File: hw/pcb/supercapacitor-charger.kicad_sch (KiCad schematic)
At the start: 11 parts, among them U2 TPS61094

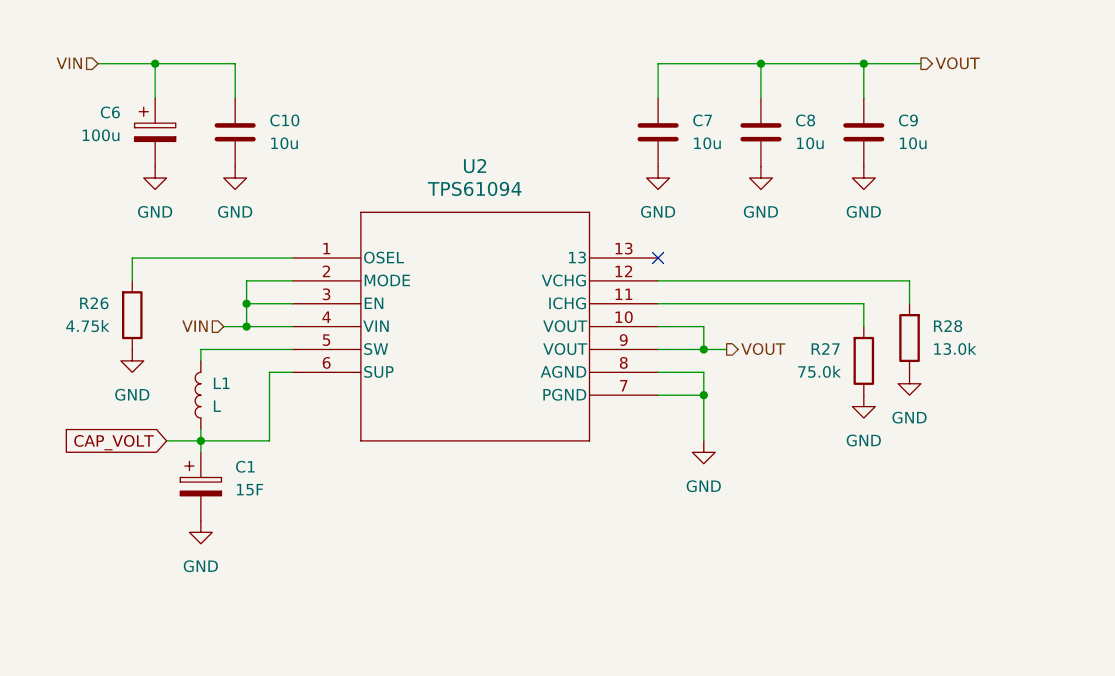
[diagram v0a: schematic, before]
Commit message: chore: updated schematics to show true part numbers
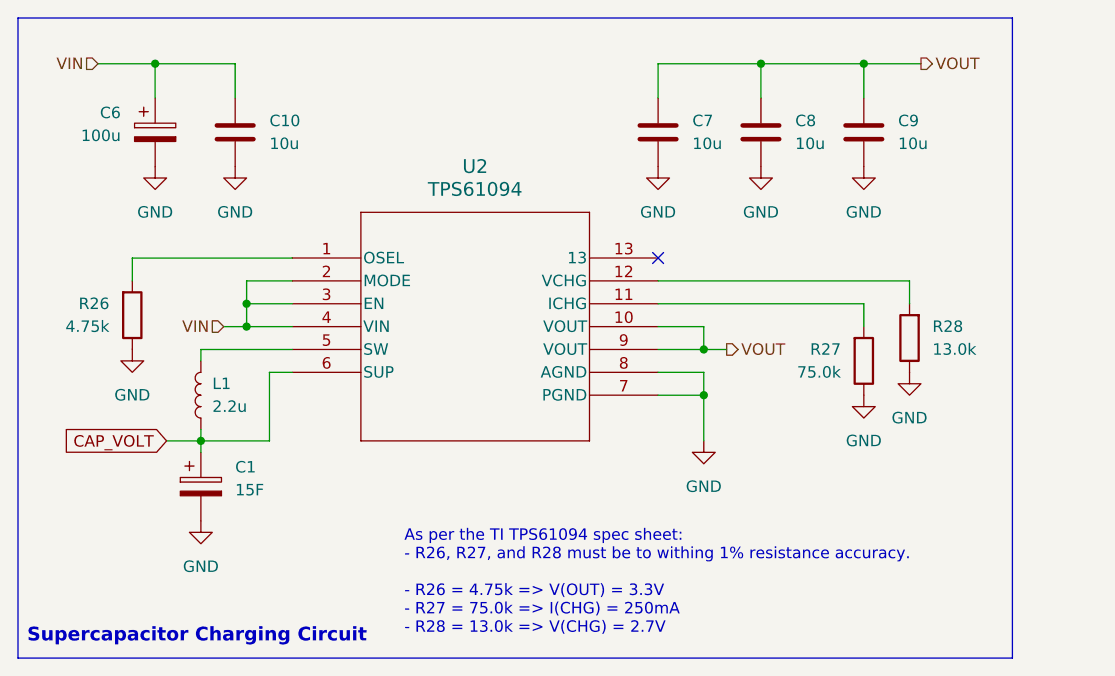
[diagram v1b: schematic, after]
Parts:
- C1: PN (none) -> MAL223051016E3
- C10, C7, C8, C9: PN (none) -> C0805C106K8PACTU
- C6: PN (none) -> UWT1A101MCL1GB
- L1: value L -> 2.2u; PN (none) -> 74438356022
- R26: PN (none) -> CPF0603F4K75C1
- R27: PN (none) -> CPF0603F75KC1
- R28: PN (none) -> CPF0603F13KC1
- U2: PN (none) -> TPS61094DSSR
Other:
- note added: "As per the TI TPS61094 spec sheet: - R26, R27, and R28 must be to withing 1% resistance accuracy. - R26 = 4.75k => V(OUT) = 3.3V - R27 = 75.0k => I(CHG) = 250mA - R28 = 13.0k => V(CHG) = 2.7V"
- note added: "Supercapacitor Charging Circuit"
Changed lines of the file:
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@@
 		(rev "RevA")
+	)
+	(rectangle
+		(start 95.25 71.12)
+		(end 205.74 142.24)
+		(stroke
+			(width 0)
+			(type default)
+		)
+		(fill
+			(type none)
+		)
+	)
+	(text "As per the TI TPS61094 spec sheet:\n- R26, R27, and R28 must be to withing 1% resistance accuracy.\n\n- R26 = 4.75k => V(OUT) = 3.3V\n- R27 = 75.0k => I(CHG) = 250mA\n- R28 = 13.0k => V(CHG) = 2.7V"
+		(exclude_from_sim no)
+		(at 138.176 128.016 0)
+		(effects
+			(font
+				(size 1.27 1.27)
+			)
+			(justify left top)
+		)
+	)
+	(text "Supercapacitor Charging Circuit"
+		(exclude_from_sim no)
+		(at 96.266 140.716 0)
+		(effects
+			(font
+				(size 1.524 1.524)
+				(thickness 0.3048)
+				(bold yes)
+			)
+			(justify left bottom)
+		)
 	)
 	(junction
@@
 			)
 		)
+		(property "PN" "C0805C106K8PACTU"
+			(at 119.38 83.82 0)
+			(hide yes)
+			(show_name no)
+			(do_not_autoplace no)
+			(effects
+				(font
+					(size 1.27 1.27)
+				)
+			)
+		)
 		(pin "1"
 		)
@@
 			)
 		)
+		(property "PN" "CPF0603F75KC1"
+			(at 189.23 109.22 0)
+			(hide yes)
+			(show_name no)
+			(do_not_autoplace no)
+			(effects
+				(font
+					(size 1.27 1.27)
+				)
+			)
+		)
 		(pin "2"
 		)
@@
 			)
 		)
+		(property "PN" "CPF0603F13KC1"
+			(at 194.31 106.68 0)
+			(hide yes)
+			(show_name no)
+			(do_not_autoplace no)
+			(effects
+				(font
+					(size 1.27 1.27)
+				)
+			)
+		)
 		(pin "2"
 		)
@@
 			)
 		)
+		(property "PN" "C0805C106K8PACTU"
+			(at 177.8 83.82 0)
+			(hide yes)
+			(show_name no)
+			(do_not_autoplace no)
+			(effects
+				(font
+					(size 1.27 1.27)
+				)
+			)
+		)
 		(pin "1"
 		)
@@
 		)
 		(property "Description" "Unpolarized capacitor"
+			(at 166.37 83.82 0)
+			(hide yes)
+			(show_name no)
+			(do_not_autoplace no)
+			(effects
+				(font
+					(size 1.27 1.27)
+				)
+			)
+		)
+		(property "PN" "C0805C106K8PACTU"
 			(at 166.37 83.82 0)
 			(hide yes)
@@
 			)
 		)
+		(property "PN" "CPF0603F4K75C1"
+			(at 107.95 104.14 0)
+			(hide yes)
+			(show_name no)
+			(do_not_autoplace no)
+			(effects
+				(font
+					(size 1.27 1.27)
+				)
+			)
+		)
 		(pin "2"
 		)
@@
 			)
 		)
+		(property "PN" "MAL223051016E3"
+			(at 115.57 123.19 0)
+			(hide yes)
+			(show_name no)
+			(do_not_autoplace no)
+			(effects
+				(font
+					(size 1.27 1.27)
+				)
+			)
+		)
 		(pin "2"
 		)
@@
 		)
 		(property "Description" ""
+			(at 146.05 105.41 0)
+			(hide yes)
+			(show_name no)
+			(do_not_autoplace no)
+			(effects
+				(font
+					(size 1.27 1.27)
+				)
+			)
+		)
+		(property "PN" "TPS61094DSSR"
 			(at 146.05 105.41 0)
 			(hide yes)
@@
 			)
 		)
-		(property "Value" "L"
+		(property "Value" "2.2u"
 			(at 116.84 114.2999 0)
 			(show_name no)
@@
 		)
 		(property "Description" "Inductor"
+			(at 115.57 113.03 0)
+			(hide yes)
+			(show_name no)
+			(do_not_autoplace no)
+			(effects
+				(font
+					(size 1.27 1.27)
+				)
+			)
+		)
+		(property "PN" "74438356022"
 			(at 115.57 113.03 0)
 			(hide yes)
@@
 			)
 		)
+		(property "PN" "C0805C106K8PACTU"
+			(at 189.23 83.82 0)
+			(hide yes)
+			(show_name no)
+			(do_not_autoplace no)
+			(effects
+				(font
+					(size 1.27 1.27)
+				)
+			)
+		)
 		(pin "1"
 		)
@@
 			(at 110.49 83.82 0)
 			(hide yes)
+			(show_name no)
+			(do_not_autoplace no)
+			(effects
+				(font
+					(size 1.27 1.27)
+				)
+			)
+		)
+		(property "PN" "UWT1A101MCL1GB"
+			(at 110.49 83.82 0)
+			(hide yes)
